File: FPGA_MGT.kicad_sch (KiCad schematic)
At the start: 2 parts

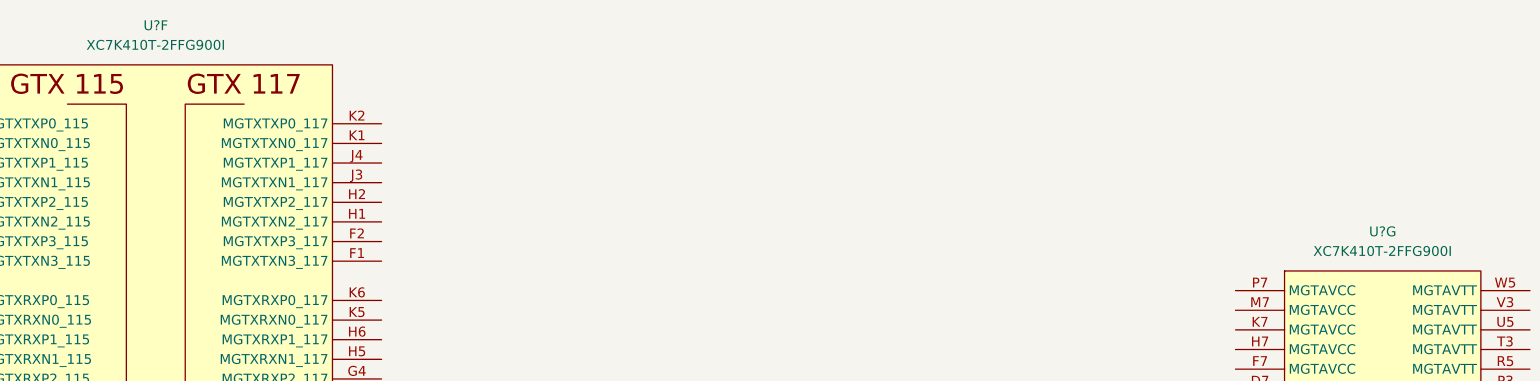
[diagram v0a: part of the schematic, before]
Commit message: Add MT41K512M8DA DDR3L
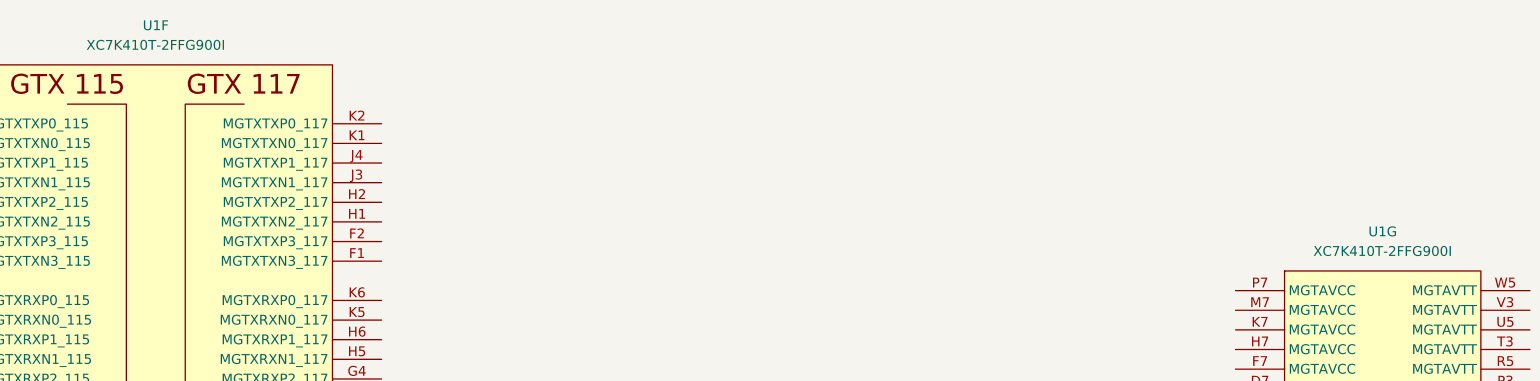
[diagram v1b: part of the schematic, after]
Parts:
- gave numbers to parts that had none: 1
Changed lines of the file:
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@@
   (symbol (lib_id "antmicroMicrocontrollers:XC7K410T-2FFG900I") (at 120.65 137.16 0) (unit 6)
     (in_bom yes) (on_board yes) (fields_autoplaced)
-    (property "Reference" "U?" (id 0) (at 120.65 66.04 0))
+    (property "Reference" "U1" (id 0) (at 120.65 66.04 0))
     (property "Value" "XC7K410T-2FFG900I" (id 1) (at 120.65 68.58 0))
     (property "Footprint" "antmicro-footprints:xc7k410t-2ffg900I" (id 2) (at 120.65 212.09 0)
@@
   (symbol (lib_id "antmicroMicrocontrollers:XC7K410T-2FFG900I") (at 279.4 125.73 0) (unit 7)
     (in_bom yes) (on_board yes) (fields_autoplaced)
-    (property "Reference" "U?" (id 0) (at 279.4 92.71 0))
+    (property "Reference" "U1" (id 0) (at 279.4 92.71 0))
     (property "Value" "XC7K410T-2FFG900I" (id 1) (at 279.4 95.25 0))
     (property "Footprint" "antmicro-footprints:xc7k410t-2ffg900I" (id 2) (at 279.4 200.66 0)

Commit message: Unify title block
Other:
- title: (none) -> K410T devboard
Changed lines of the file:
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@@
   (paper "A3")
   (title_block
-    (comment 1 "www.antmicro.com")
-    (comment 2 "Antmicro Ltd")
+    (title "K410T devboard")
+    (date "2022-12-20")
+    (rev "0.0.99")
   )
   (symbol (lib_id "antmicroMicrocontrollers:XC7K410T-2FFG900I") (at 120.65 137.16 0) (unit 6)
